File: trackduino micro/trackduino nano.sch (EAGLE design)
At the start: 27 parts, among them IC2 74AHC1G125DBV, SW1 SPST_TACT-KMR2, U1 ATMEGA168, Y1 16MHZ

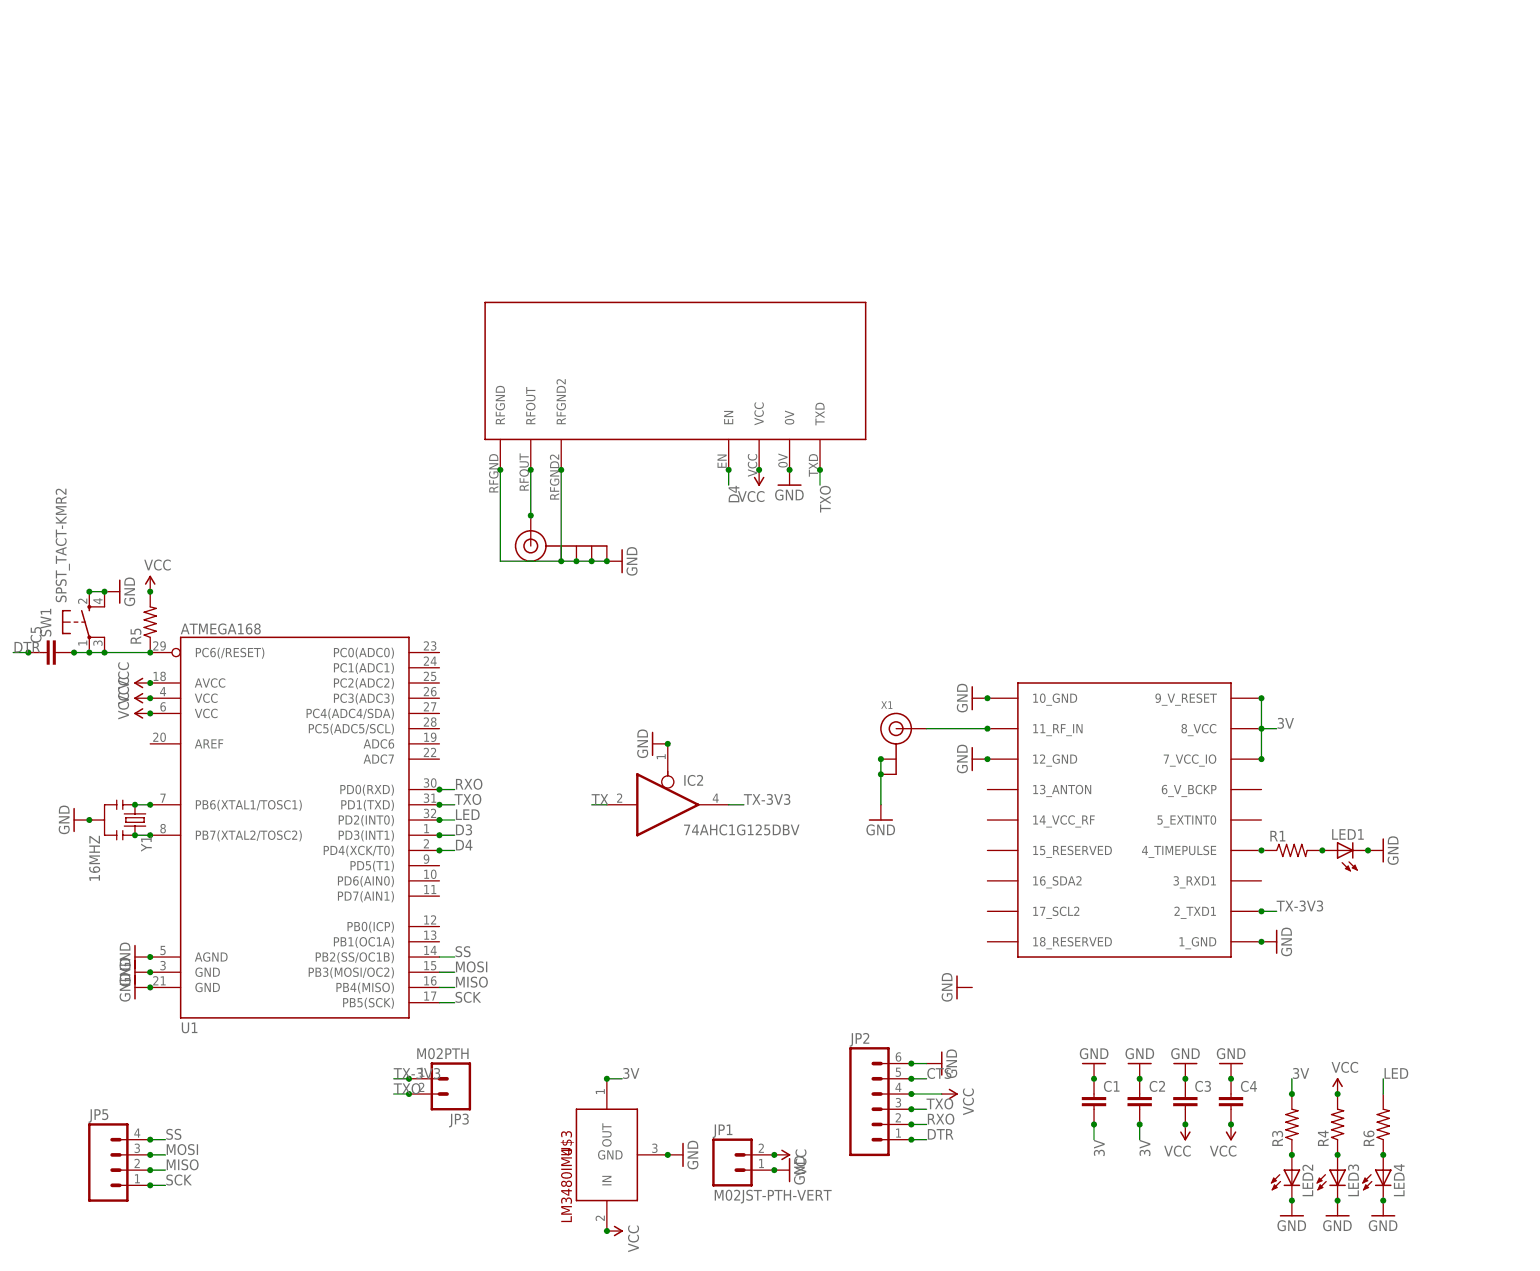
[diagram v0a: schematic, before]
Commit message: removed level shifters
removed unnecessary 5v level shifters from boards.
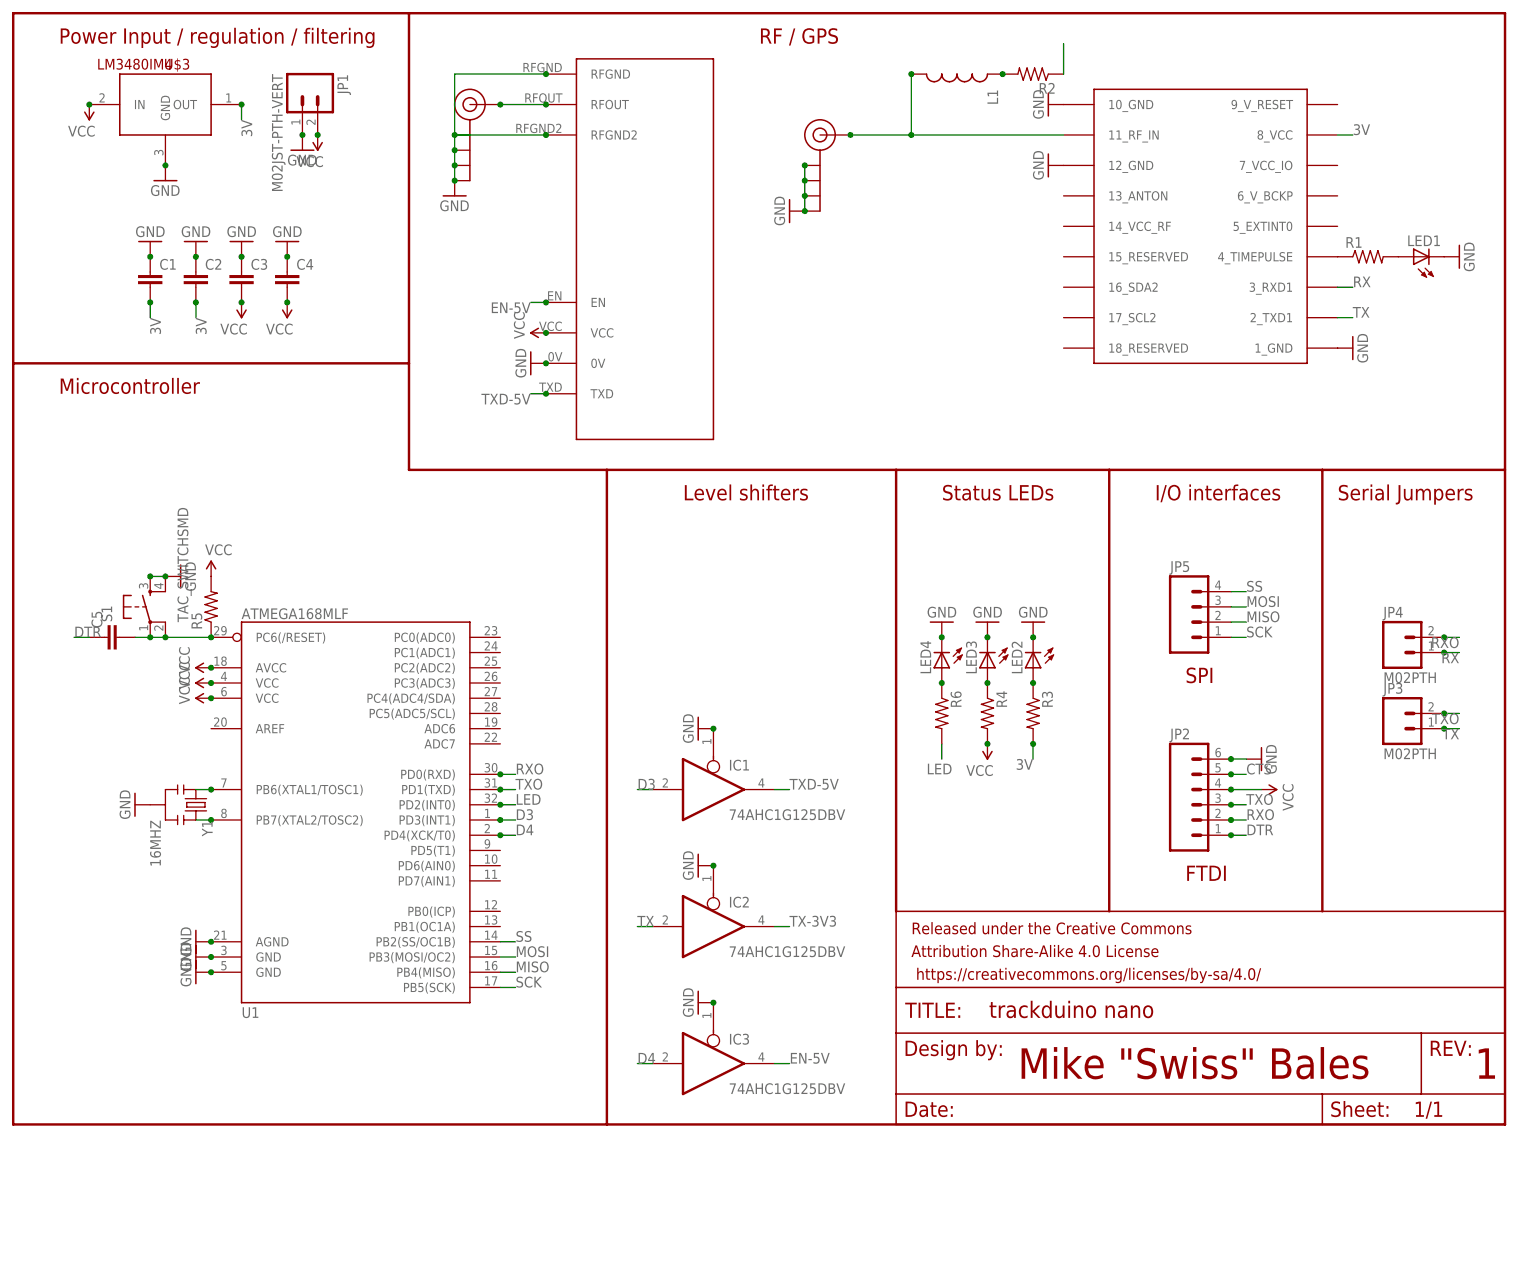
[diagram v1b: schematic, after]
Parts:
- removed SW1: SPST_TACT-KMR2, adafruit:SPST_TACT-KMR2
- removed X1: (no value), adafruit:ANTENNA_U.FL
- added FRAME1: FRAME-LETTER, SparkFun-Aesthetics:FRAME-LETTER
- added IC1, IC3: 74AHC1G125DBV, 74xx-little-us:74AHC1G125DBV
- added J$2: SMA_EDGE, SparkFun-Connectors:SMA_EDGE
- added JP4: M02PTH, SparkFun-Connectors:M02PTH
- added L1: (no value), SparkFun-Passives:INDUCTOR0805
- added R2: (no value), SparkFun-Resistors:RESISTOR0805-RES
- added S1: TAC_SWITCHSMD, SparkFun-Electromechanical:TAC_SWITCHSMD
- U1: value ATMEGA168 -> ATMEGA168MLF; device SparkFun-DigitalIC:ATMEGA168 -> SparkFun-DigitalIC:ATMEGA168MLF
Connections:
- new net EN-5V: IC3A.O, U$2.EN
- new net N$4: R2.1
- new net N$5: L1.1, R2.2
- new net RX: JP4.1, U$1.3_RXD1
- new net TXD-5V: IC1A.O, U$2.TXD
- net 3V: no longer U$1.7_VCC_IO, U$1.9_V_RESET
- net D3: now also IC1A.I
- net D4: now also IC3A.I; no longer U$2.EN
- net GND: now also IC1A.OE, IC3A.OE, J$2.GND@0, J$2.GND@1, J$2.GND@2, J$2.GND@3, S1.3, S1.4; no longer SW1.S, SW1.S1, X1.GND@0, X1.GND@1
- net N$6: now also J$2.SIGNAL, L1.2; no longer X1.SIGNAL
- net N$9: now also S1.1, S1.2; no longer SW1.P, SW1.P1
- net RXO: now also JP4.2
- net TX: now also JP3.1, U$1.2_TXD1
- net TX-3V3: no longer JP3.1, U$1.2_TXD1
- net TXO: no longer U$2.TXD
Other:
- note added: "1"
- note added: "FTDI"
- note added: "I/O interfaces"
- note added: "Level shifters"
- note added: "Microcontroller"
- note added: "Mike "Swiss" Bales"
- note added: "Power Input / regulation / filtering"
- note added: "RF / GPS"
- note added: "SPI"
- note added: "Serial Jumpers"
- note added: "Status LEDs"
- moved on the sheet: C1, C2, C3, C4, C5, IC2, JP1, JP2, JP3, JP5, LED1, LED2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
